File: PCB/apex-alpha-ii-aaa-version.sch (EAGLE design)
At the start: 31 parts, among them IC1 CC430F5135, X2 SMA-142-0701-801/806, Y1 26MHz

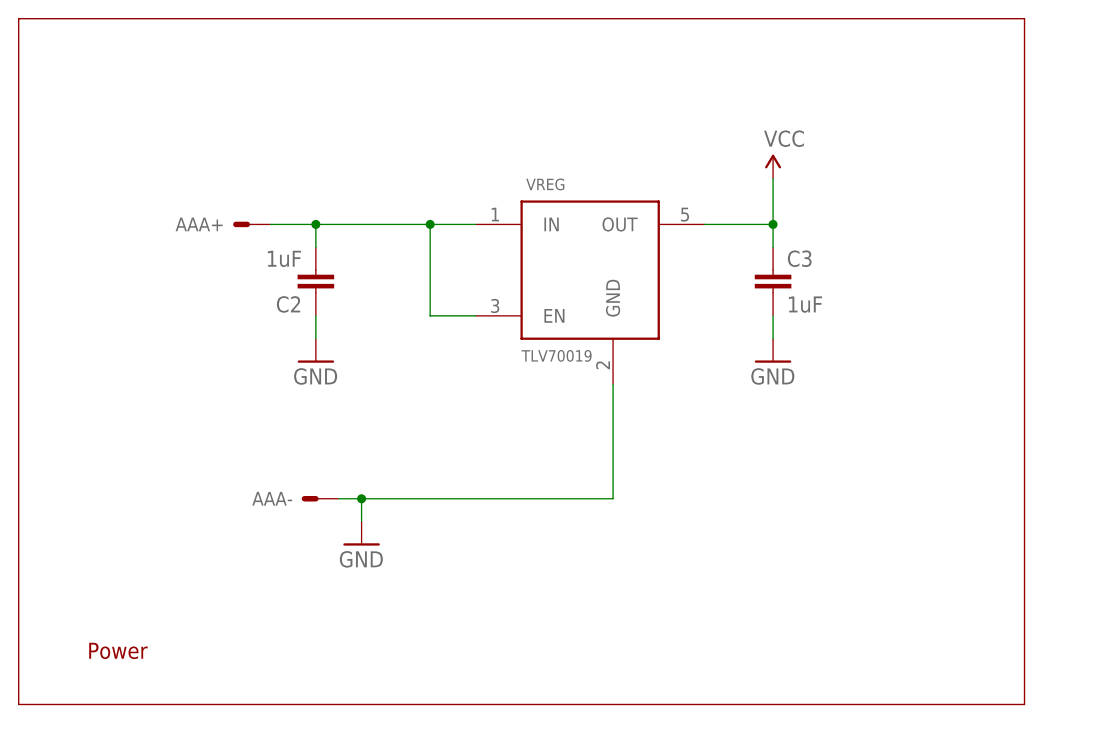
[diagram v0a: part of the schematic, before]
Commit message: Changed to TLV70019 linear reg for a 3V battery
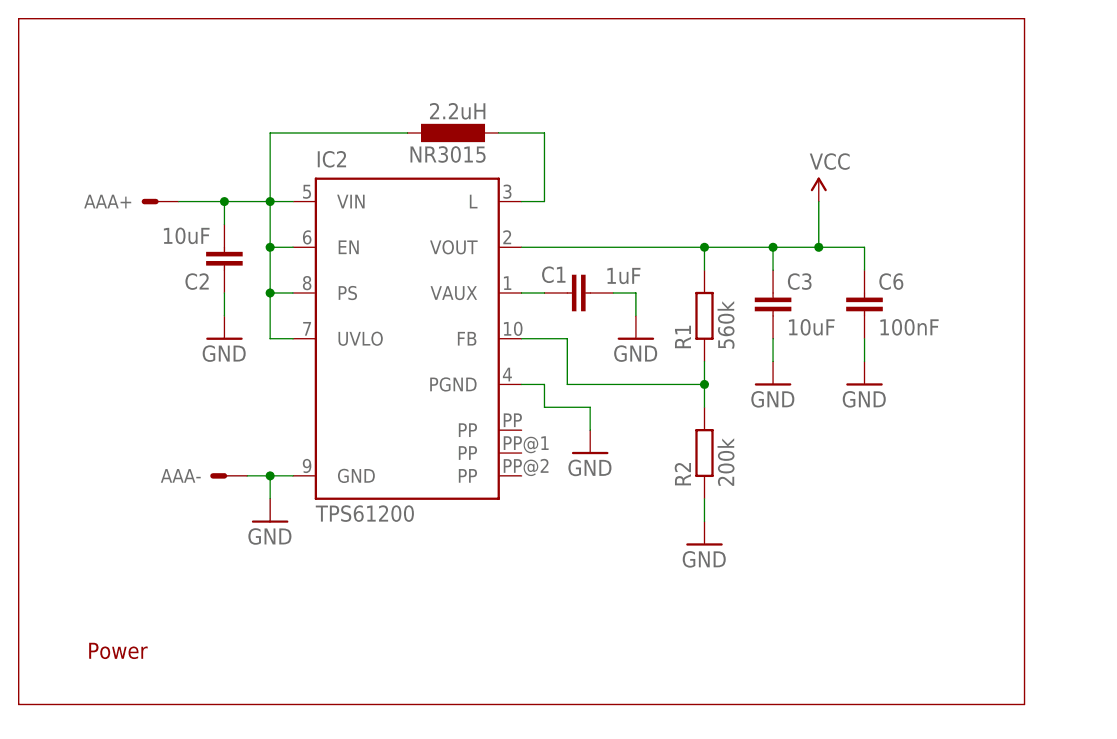
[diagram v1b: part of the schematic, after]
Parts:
- removed VREG: TLV70019, !danielparts:TLV70019
- added C1: 1uF, apex:CAP0402-CAP
- added C6: 100nF, apex:CAP0402-CAP
- added IC2: TPS61200, texas:TPS61200
- added NR3015: 2.2uH, apex:NR3015
- added R1: 560k, apex:R-EU_R0402
- added R2: 200k, apex:R-EU_R0402
- C2, C3: value 1uF -> 10uF
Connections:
- new net N$1: AAA+.S, C2.2, IC2.EN, IC2.PS, IC2.UVLO, IC2.VIN, NR3015.1
- new net N$4: IC2.FB, R1.1, R2.2
- new net N$5: C1.1, IC2.VAUX
- net GND: now also C1.2, C6.2, IC2.GND, IC2.PGND, R2.1; no longer VREG.GND
- net N$3: now also IC2.L, NR3015.2; no longer AAA+.S, C2.2, VREG.EN, VREG.IN
- net VCC: now also C6.1, IC2.VOUT, R1.2; no longer VREG.OUT
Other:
- moved on the sheet: AAA+, AAA-, C2, C3

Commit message: AAA version fully laid out.
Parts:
- removed JP1: APEXHAB-LOGO_APEXHAB-SMALL, apex:APEXHAB-LOGO_APEXHAB-SMALL
- TP1, TP2: value PTR1B2,54 -> PTR1B1,27; device testpad:PTR1B2,54 -> testpad:PTR1B1,27
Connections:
- new net VEE: C11.1, C12.1, C13.1, C14.1, C15.1, IC1.27, IC1.28, IC1.31, IC1.32, IC1.34, U$2.2
- net VCC: no longer C11.1, C12.1, C13.1, C14.1, C15.1, IC1.27, IC1.28, IC1.31, IC1.32, IC1.34, U$2.2

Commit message: Nearly finished routing... committing before I lose it all.
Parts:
- U$3: device apex:LED_0805 -> apex:LED_0603
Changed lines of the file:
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@@
 <part name="GND19" library="apex" deviceset="GND" device=""/>
 <part name="P+9" library="apex" deviceset="VCC" device=""/>
-<part name="U$3" library="apex" deviceset="LED" device="_0805" value="STATUS"/>
+<part name="U$3" library="apex" deviceset="LED" device="_0603" value="STATUS"/>
 <part name="GND20" library="apex" deviceset="GND" device=""/>
 <part name="GND21" library="apex" deviceset="GND" device=""/>

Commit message: Finished! I think.
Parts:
- U$3: device apex:LED_0603 -> apex:LED
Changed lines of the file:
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@@
 <part name="GND19" library="apex" deviceset="GND" device=""/>
 <part name="P+9" library="apex" deviceset="VCC" device=""/>
-<part name="U$3" library="apex" deviceset="LED" device="_0603" value="STATUS"/>
+<part name="U$3" library="apex" deviceset="LED" device="" value="STATUS"/>
 <part name="GND20" library="apex" deviceset="GND" device=""/>
 <part name="GND21" library="apex" deviceset="GND" device=""/>

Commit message: New PCB layout etc.
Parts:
- added C19: 4.7uF, apex:CAP0805
- AAA: value SMD-BATTERY-HOLDER-AAA -> KEYSTONE-2466-THROUGH-HOLE-BATTERY-HOLDER-AAA; device apex:SMD-BATTERY-HOLDER-AAA -> apex:KEYSTONE-2466-THROUGH-HOLE-BATTERY-HOLDER-AAA
- C10: value 10uF -> 1uF
- C2, C3: device apex:CAP0402-CAP -> apex:CAP0805
- C9: value 10uF -> 100nF
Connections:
- net GND: now also C19.2, IC2.PP, IC2.PP@1, IC2.PP@2
- net VCC: now also C19.1
